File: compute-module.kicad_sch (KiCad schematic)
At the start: 9 parts

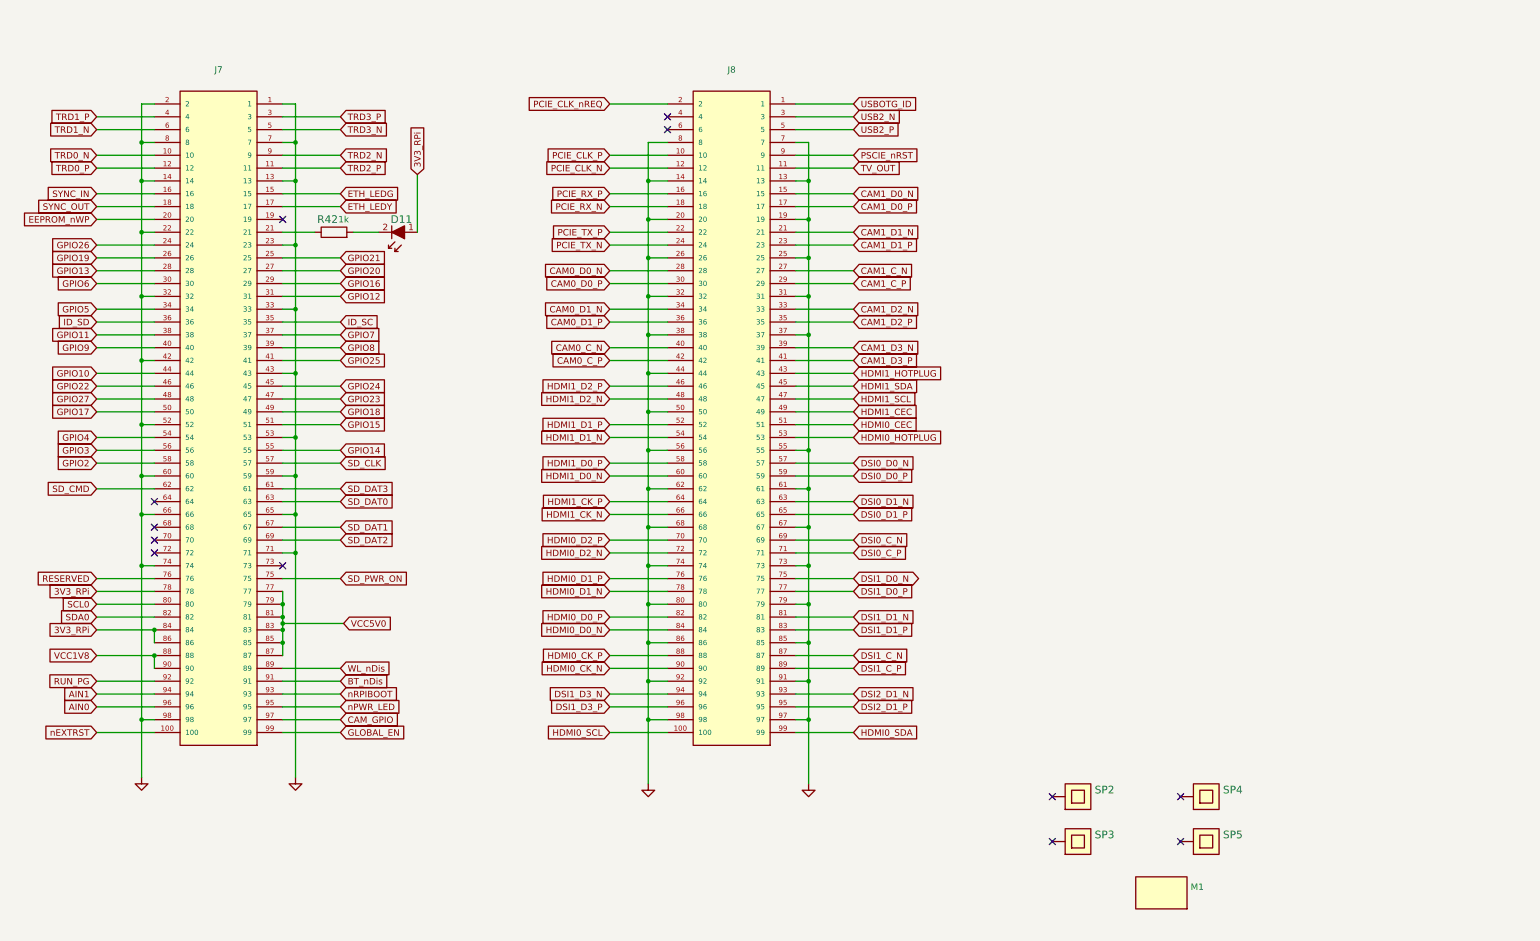
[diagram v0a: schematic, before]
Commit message: Exchanged flyback to CUI DCDC converter on schematics. Added logos.
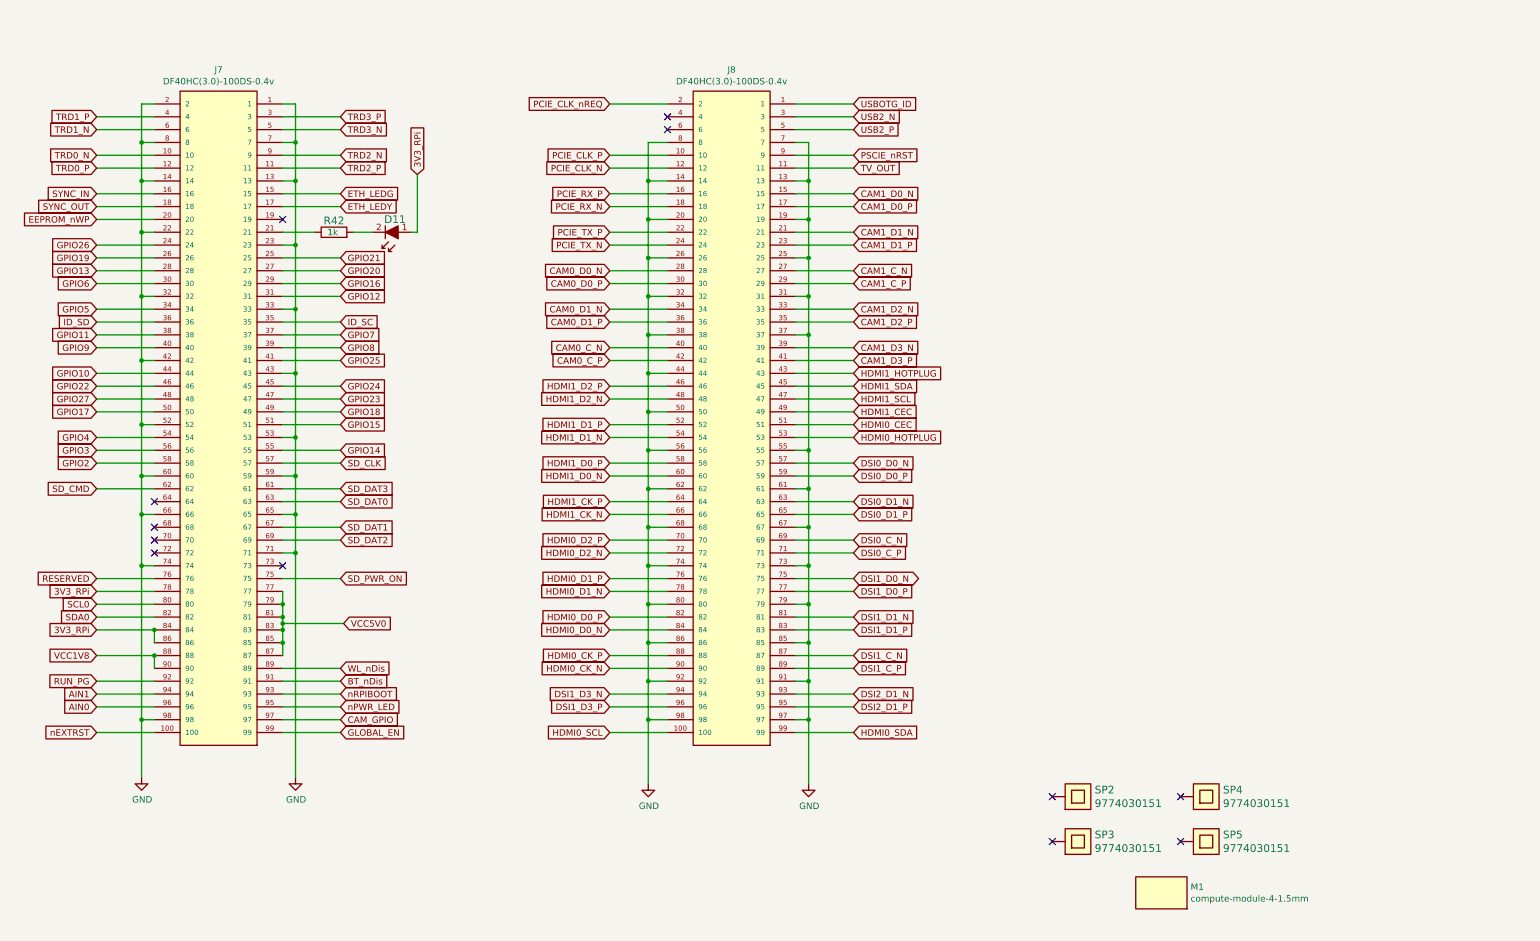
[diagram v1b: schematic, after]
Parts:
- D11: value (none) -> KP-1608CGCK; footprint scalenode-footprints: -> scalenode-footprints:LED_0603
- J7, J8: value (none) -> DF40HC(3.0)-100DS-0.4v; footprint scalenode-footprints: -> scalenode-footprints:DF40HC-3.0-100DS-0.4v
- M1: value (none) -> compute-module-4-1.5mm; footprint scalenode-footprints: -> scalenode-footprints:compute-module-4-1.5mm
- R42: value (none) -> R_1k_0603; footprint scalenode-footprints: -> scalenode-footprints:0603-res
- SP2, SP3, SP4, SP5: value (none) -> 9774030151; footprint scalenode-footprints: -> scalenode-footprints:9774030151
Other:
- moved on the sheet: D11

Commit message: Added text fields with schematic descriptions
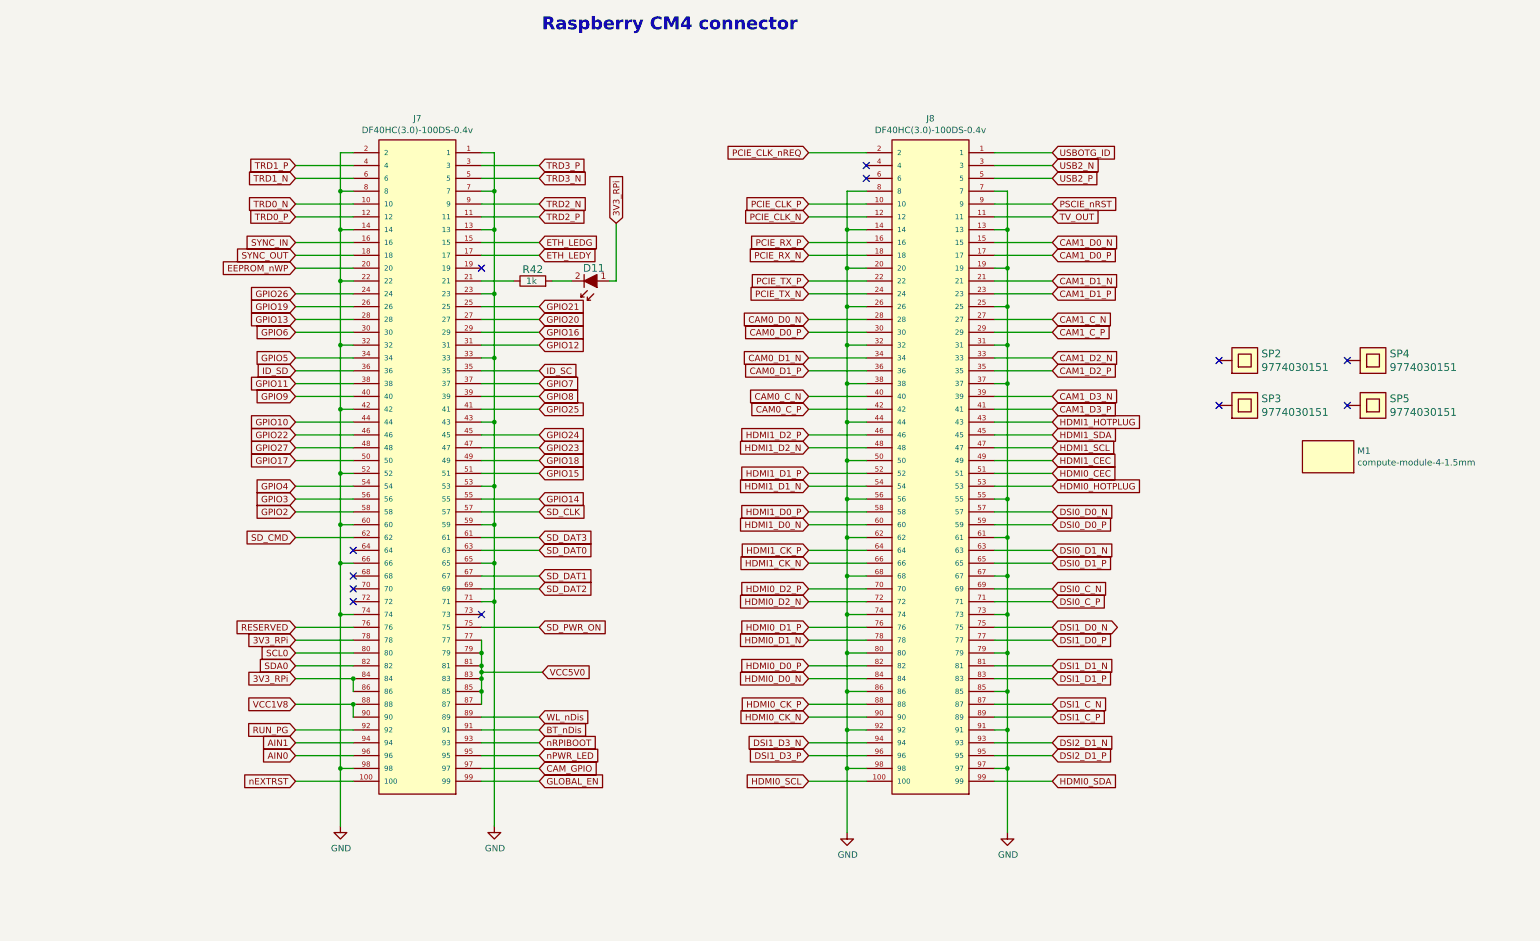
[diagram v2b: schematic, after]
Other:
- note added: "Raspberry CM4 connector"
- moved on the sheet: D11, J7, J8, M1, R42, SP2, SP3, SP4, SP5

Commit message: Implemented changes from rev 1.0.4. New components initial placement
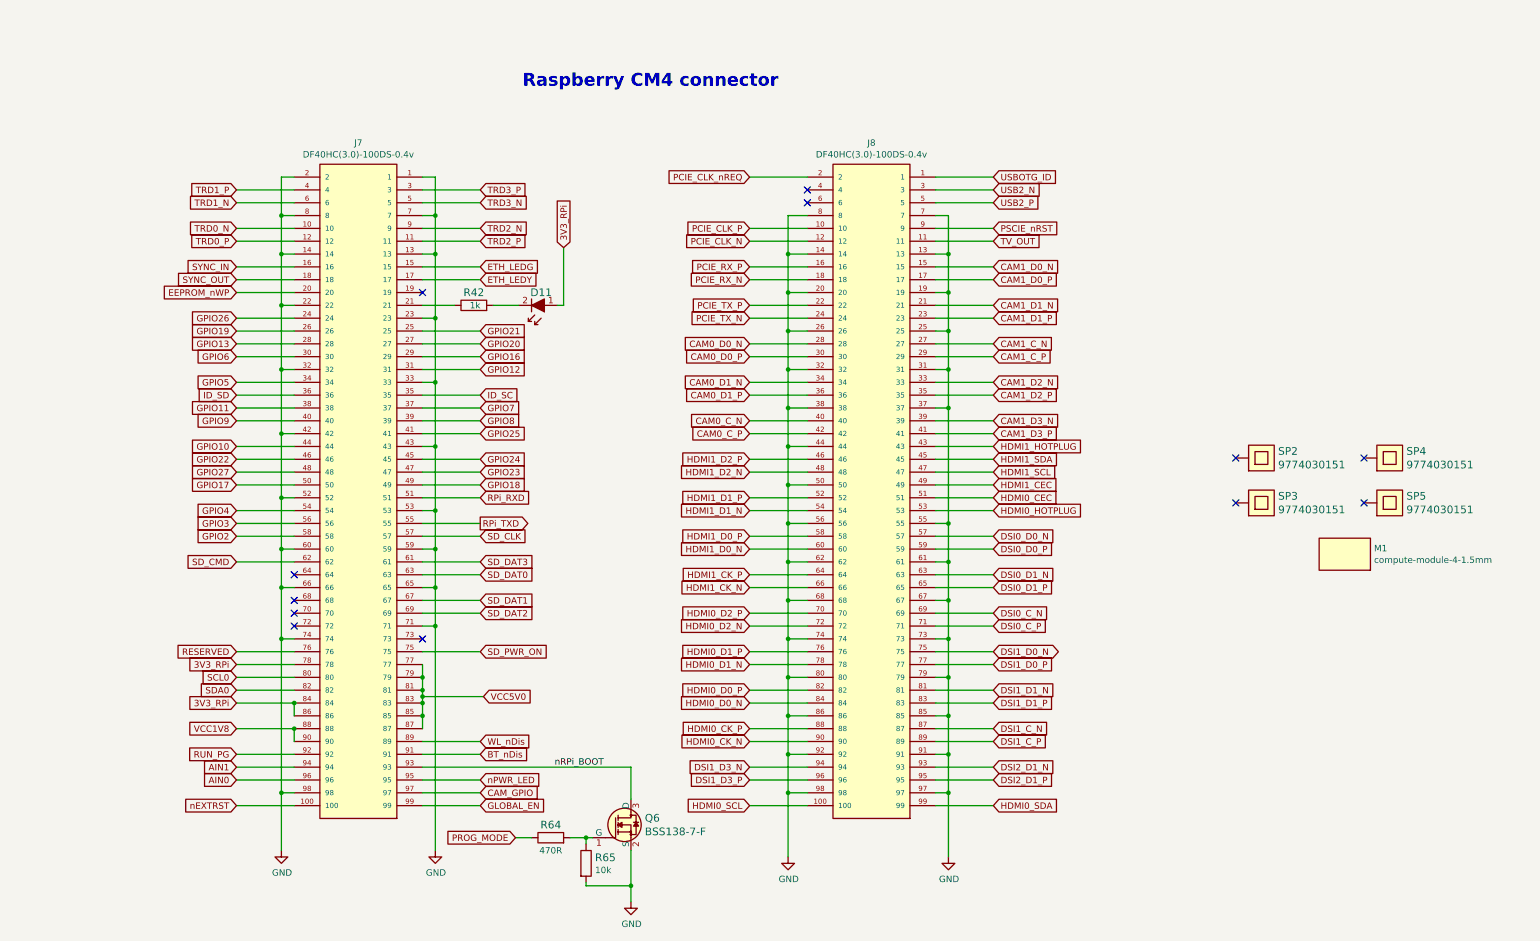
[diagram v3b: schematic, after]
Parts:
- added Q6: BSS138-7-F, scalenode-footprints:SOT-23-3, symbol scalenode:BSS138-7-F
- added R64: R_470R_0402, scalenode-footprints:0402-res, symbol scalenode:R_470R_0402
- added R65: R_10k_0402, scalenode-footprints:0402-res, symbol scalenode:R_10k_0402
- D11: value KP-1608CGCK -> 598-8D80-107F; footprint scalenode-footprints:LED_0603 -> scalenode-footprints:LED_0603_R; symbol scalenode:KP-1608CGCK -> scalenode:598-8D80-107F; MPN KP-1608CGCK -> 598-8D80-107F; Manufacturer KINGBRIGHT -> DIALIGHT
- J7, J8: MPN (none) -> DF40HC(3.0)-100DS-0.4v(51
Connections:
- net GND: now also Q6.2 (S), R65.2
- net GPIO14 renamed RPi_TXD
- net GPIO15 renamed RPi_RXD
- net nRPIBOOT renamed nRPi_BOOT
- net nRPi_BOOT: now also Q6.3 (D)
- new net: Q6.1 (G), R64.2, R65.1
- new net PROG_MODE: R64.1
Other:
- moved on the sheet: D11, J7, J8, M1, R42, SP2, SP3, SP4, SP5

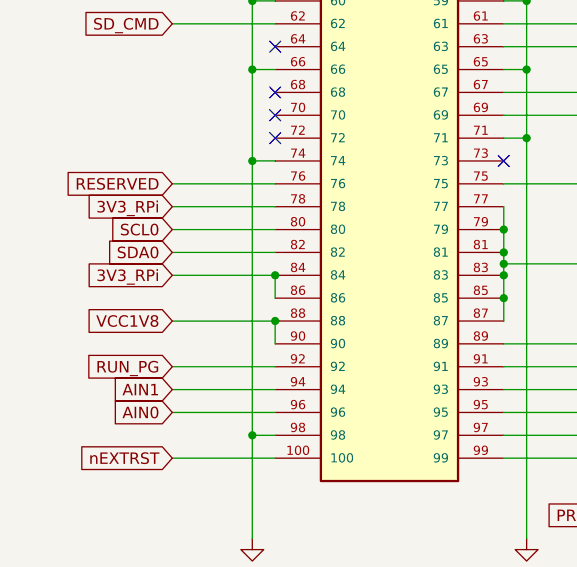
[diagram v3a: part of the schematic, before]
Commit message: Corrected footprints. Adjusted position of testpoints. Cleared DRC
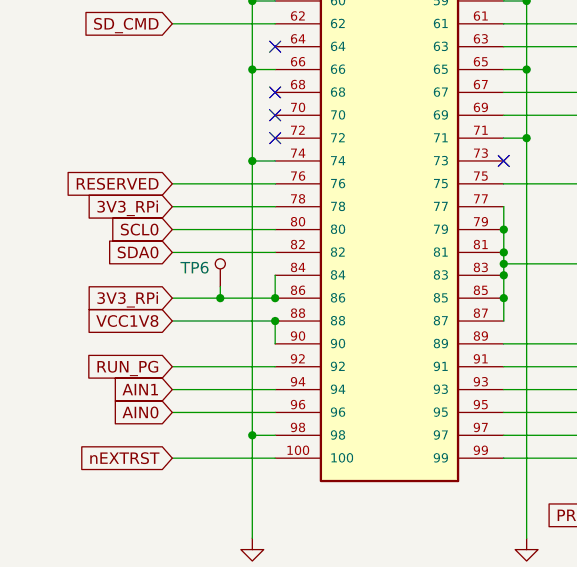
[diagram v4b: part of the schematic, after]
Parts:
- added TP6: TP_SMD1MM, scalenode-footprints:Testpoint_smd_1mm, symbol scalenode:TP_SMD1MM
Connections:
- net 3V3_RPi: now also TP6.1

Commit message: Corrected R33. Increased distance between L1 and L2. loclib
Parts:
- J7, J8: footprint scalenode-footprints:DF40HC-3.0-100DS-0.4v -> scalenode-footprints:DF40HC(3.0)-100DS-0.4v
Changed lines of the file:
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@@
-(kicad_sch
-    (version 20211123)
-    (generator eeschema)
-    (paper "A3")
-    (title_block
-        (title "Scalenode")
-        (rev "1.0.4"))
+(kicad_sch (version 20211123) (generator eeschema)
+  (paper "A3")
+  (title_block
+    (title "Scalenode")
+    (rev "1.0.4")
+  )

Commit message: Rename project files
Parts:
- D11: footprint scalenode-footprints:LED_0603_R -> scalenode-cm4-baseboard-footprints:LED_0603_R; symbol scalenode:598-8D80-107F -> scalenode-cm4-baseboard:598-8D80-107F
- J7, J8: footprint scalenode-footprints:DF40HC(3.0)-100DS-0.4v -> scalenode-cm4-baseboard-footprints:DF40HC(3.0)-100DS-0.4v; symbol scalenode:DF40HC(3.0)-100DS-0.4v -> scalenode-cm4-baseboard:DF40HC(3.0)-100DS-0.4v
- M1: footprint scalenode-footprints:compute-module-4-1.5mm -> scalenode-cm4-baseboard-footprints:compute-module-4-1.5mm; symbol scalenode:compute-module-4-1.5mm -> scalenode-cm4-baseboard:compute-module-4-1.5mm
- Q6: footprint scalenode-footprints:SOT-23-3 -> scalenode-cm4-baseboard-footprints:SOT-23-3; symbol scalenode:BSS138-7-F -> scalenode-cm4-baseboard:BSS138-7-F
- R42: footprint scalenode-footprints:0603-res -> scalenode-cm4-baseboard-footprints:0603-res; symbol scalenode:R_1k_0603 -> scalenode-cm4-baseboard:R_1k_0603
- R64: footprint scalenode-footprints:0402-res -> scalenode-cm4-baseboard-footprints:0402-res; symbol scalenode:R_470R_0402 -> scalenode-cm4-baseboard:R_470R_0402
- R65: footprint scalenode-footprints:0402-res -> scalenode-cm4-baseboard-footprints:0402-res; symbol scalenode:R_10k_0402 -> scalenode-cm4-baseboard:R_10k_0402
- SP2, SP3, SP4, SP5: footprint scalenode-footprints:9774030151 -> scalenode-cm4-baseboard-footprints:9774030151; symbol scalenode:9774030151 -> scalenode-cm4-baseboard:9774030151
- TP6: footprint scalenode-footprints:Testpoint_smd_1mm -> scalenode-cm4-baseboard-footprints:Testpoint_smd_1mm; symbol scalenode:TP_SMD1MM -> scalenode-cm4-baseboard:TP_SMD1MM
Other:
- title: Scalenode -> Scalenode CM4 Baseboard
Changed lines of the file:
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@@
-(kicad_sch
-    (version 20211123)
-    (generator eeschema)
-    (paper "A3")
-    (title_block
-        (title "Scalenode")
-        (rev "1.1.0"))
+(kicad_sch (version 20211123) (generator eeschema)
+  (paper "A3")
+  (title_block
+    (title "Scalenode CM4 Baseboard")
+    (rev "1.1.0")
+  )
